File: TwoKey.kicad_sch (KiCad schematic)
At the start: 34 parts, among them J1 USB_C_Receptacle_USB2.0, SW1 SW_SPST, SW2 SW_SPST, SW3 BOOTSEL, SW4 RESET, U1 AMS1117-3.3, U2 W25Q128JVS, U3 RP2040TR7, X1 OSC

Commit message: Condenced items into initial pcb
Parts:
- removed SW4: RESET, TwoKey:DTSL-61N-V, symbol TwoKey:DTSL-61N-V
- SW1, SW2: footprint keyswitches:Kailh_socket_MX_optional -> (none)
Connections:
- net COL1: now also SW1.2 (B); no longer SW1.1 (A)
- net COL2: now also SW2.2 (B); no longer SW2.1 (A)
- net at D2.2 (A): now also SW2.1 (A); no longer SW2.2 (B)
- net at D1.2 (A): now also SW1.1 (A); no longer SW1.2 (B)
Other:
- moved on the sheet: C4, R3, SW3, U2

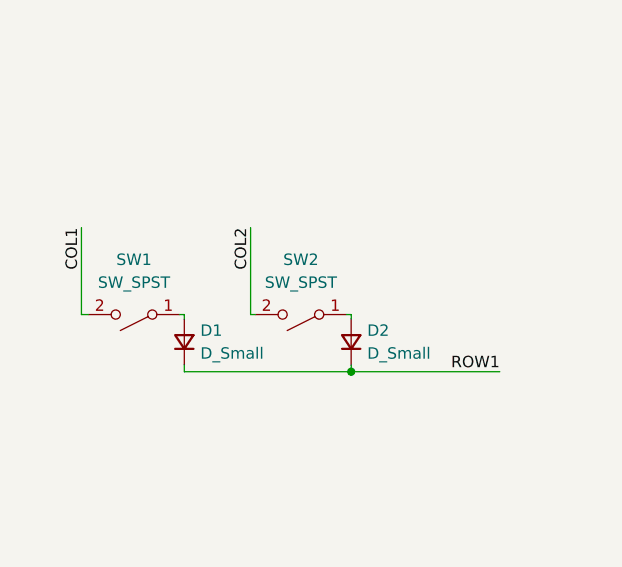
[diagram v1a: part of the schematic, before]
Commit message: Readjusted more componenets (DRC not passing)
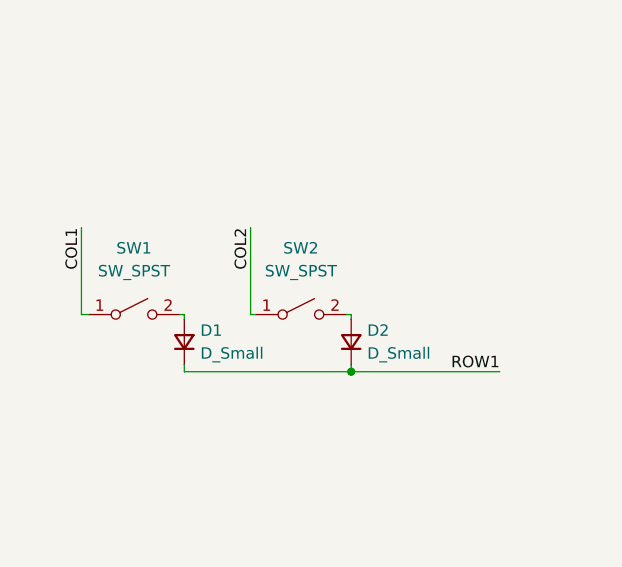
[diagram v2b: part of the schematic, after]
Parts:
- SW1, SW2: footprint (none) -> keyswitches:Kailh_socket_MX
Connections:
- net COL1: now also SW1.1 (A); no longer SW1.2 (B)
- net COL2: now also SW2.1 (A); no longer SW2.2 (B)
- net at D2.2 (A): now also SW2.2 (B); no longer SW2.1 (A)
- net at D1.2 (A): now also SW1.2 (B); no longer SW1.1 (A)
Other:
- moved on the sheet: SW1, SW2
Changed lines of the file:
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@@
     (pin "2")
   )
-  (symbol (lib_id "Switch:SW_SPST") (at 53.086 148.336 180) (unit 1)
+  (symbol (lib_id "Switch:SW_SPST") (at 53.086 148.336 0) (unit 1)
     (in_bom yes) (on_board yes) (fields_autoplaced)
-    (property "Reference" "SW2" (id 0) (at 53.086 142.24 0))
-    (property "Value" "SW_SPST" (id 1) (at 53.086 144.78 0))
-    (property "Footprint" "" (id 2) (at 53.086 148.336 0)
+    (property "Reference" "SW2" (id 0) (at 53.086 140.97 0))
+    (property "Value" "SW_SPST" (id 1) (at 53.086 143.51 0))
+    (property "Footprint" "keyswitches:Kailh_socket_MX" (id 2) (at 53.086 148.336 0)
       (effects (font (size 1.27 1.27)) hide)
     )
@@
     (pin "2")
   )
-  (symbol (lib_id "Switch:SW_SPST") (at 34.544 148.336 180) (unit 1)
+  (symbol (lib_id "Switch:SW_SPST") (at 34.544 148.336 0) (unit 1)
     (in_bom yes) (on_board yes) (fields_autoplaced)
-    (property "Reference" "SW1" (id 0) (at 34.544 142.24 0))
-    (property "Value" "SW_SPST" (id 1) (at 34.544 144.78 0))
-    (property "Footprint" "" (id 2) (at 34.544 148.336 0)
-      (effects (font (size 1.27 1.27)) hide)
-    )
+    (property "Reference" "SW1" (id 0) (at 34.544 140.97 0))
+    (property "Value" "SW_SPST" (id 1) (at 34.544 143.51 0))
+    (property "Footprint" "keyswitches:Kailh_socket_MX" (id 2) (at 34.544 148.336 0)
+      (effects (font (size 1.27 1.27)) hide)
+    )

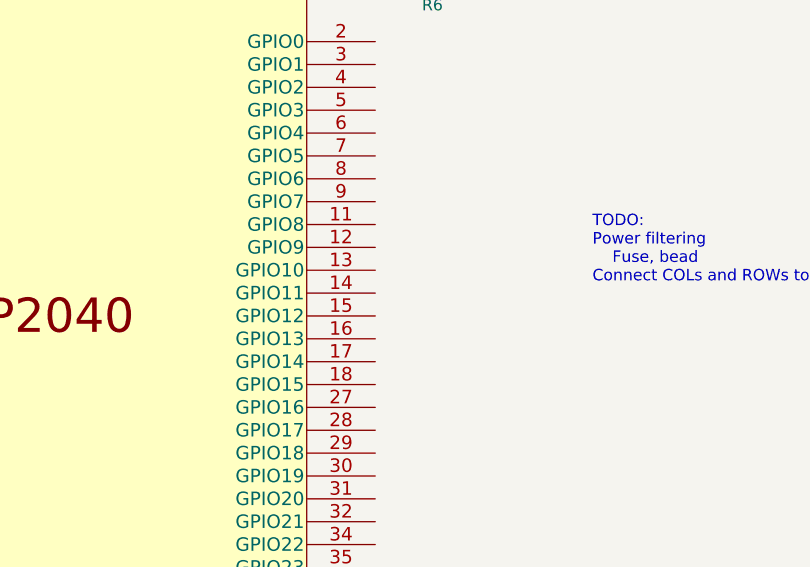
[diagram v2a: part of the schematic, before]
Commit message: Finished routing of all traces
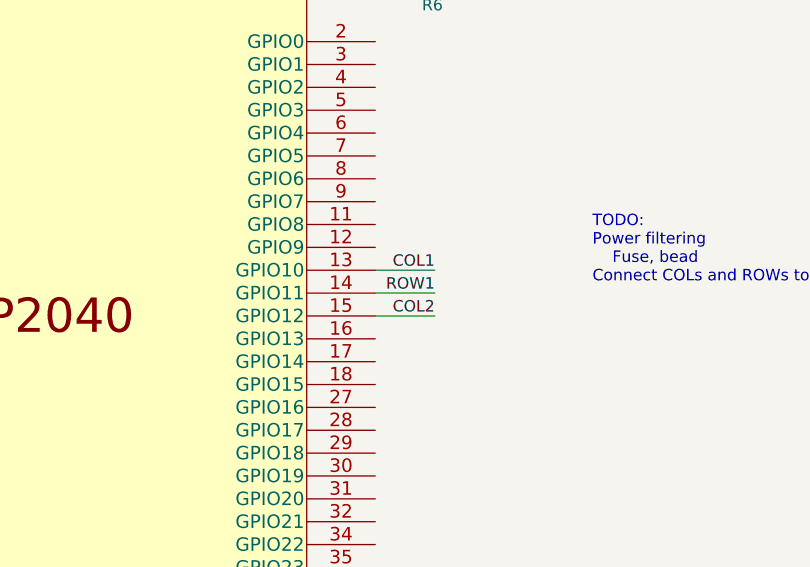
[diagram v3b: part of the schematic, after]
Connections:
- net COL1: now also U3.13 (GPIO10)
- net COL2: now also U3.15 (GPIO12)
- net ROW1: now also U3.14 (GPIO11)
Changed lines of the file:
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@@
+    (stroke (width 0) (type default) (color 0 0 0 0))
+  )
+  (wire (pts (xy 222.758 90.17) (xy 229.362 90.17))
     (stroke (width 0) (type default) (color 0 0 0 0))
   )
@@
     (stroke (width 0) (type default) (color 0 0 0 0))
   )
+  (wire (pts (xy 222.758 95.25) (xy 229.362 95.25))
+    (stroke (width 0) (type default) (color 0 0 0 0))
+  )
   (wire (pts (xy 51.308 39.37) (xy 54.102 39.37))
     (stroke (width 0) (type default) (color 0 0 0 0))
@@
   )
   (wire (pts (xy 110.998 36.83) (xy 110.998 38.354))
+    (stroke (width 0) (type default) (color 0 0 0 0))
+  )
+  (wire (pts (xy 222.758 92.71) (xy 229.362 92.71))
     (stroke (width 0) (type default) (color 0 0 0 0))
   )
@@
     (effects (font (size 1.27 1.27)) (justify right bottom))
   )
+  (label "ROW1" (at 229.362 92.71 180)
+    (effects (font (size 1.27 1.27)) (justify right bottom))
+  )
   (label "XOUT" (at 279.146 143.002 180)
     (effects (font (size 1.27 1.27)) (justify right bottom))
@@
     (effects (font (size 1.27 1.27)) (justify left bottom))
   )
+  (label "COL2" (at 229.362 95.25 180)
+    (effects (font (size 1.27 1.27)) (justify right bottom))
+  )
   (label "USB_DP" (at 241.3 54.61 180)
     (effects (font (size 1.27 1.27)) (justify right bottom))
@@
     (effects (font (size 1.27 1.27)) (justify right bottom))
   )
+  (label "COL1" (at 229.362 90.17 180)
+    (effects (font (size 1.27 1.27)) (justify right bottom))
+  )
